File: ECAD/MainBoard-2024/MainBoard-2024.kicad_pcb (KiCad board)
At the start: 2 copper layers, 100 x 100 mm, 65 parts, among them J1 XT60, J10 Conn_01x02, J11 Conn_01x03, J12 Conn_01x04, J13 Conn_01x03, J14 Conn_01x03, J15 Conn_01x02, J16 XT30, J17 XT30, J18 Conn_01x02, J2 Conn_01x04, J20 BAU, J21 BAU, J22 Conn_01x04, J23 Conn_01x02, J26 BAU, J27 BAU, J28 Conn_01x02, J29 Conn_01x02, J3 ConStep1, J30 Conn_01x03, J4 Conn_01x02, J5 ConStep1, J6 ConStep1, J7 XT30, J8 Conn_01x02, J9 Conn_01x02, K2 FINDER-36.11, U1 Teensy3.5_All_Pins, U2 R-78B3.3-2.0, U3 R-78B12-2.0, U4 R-78B5.0-2.0

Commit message: Clean positions
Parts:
- removed J16, J17: XT30, Connector_AMASS:AMASS_XT30U-F_1x02_P5.0mm_Vertical
- moved J27 84.2 mm to (187.3, 70.1)
- moved J20 83.1 mm to (187.3, 58.4)
- moved J26 83.1 mm to (196.9, 58.4)
- moved C4 48.3 mm to (165.1, 68.6)
- moved C6 48.3 mm to (165.1, 58.4)
- moved K2 36.0 mm to (142.3, 133.2), turned to 0 degrees
- moved J1 29.1 mm to (165.6, 137.6), turned to -90 degrees
- moved J21 27.3 mm to (187.5, 141.2)
- moved D1 21.4 mm to (187.2, 102.6)
- moved D3 21.4 mm to (188.5, 107.7)
- moved D5 21.4 mm to (187.2, 100.1)
- moved D6 21.4 mm to (187.2, 95.0)
- moved D8 21.4 mm to (193.5, 107.7)
- moved R1 21.4 mm to (192.4, 102.6)
- moved R17 21.4 mm to (190.8, 107.7)
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
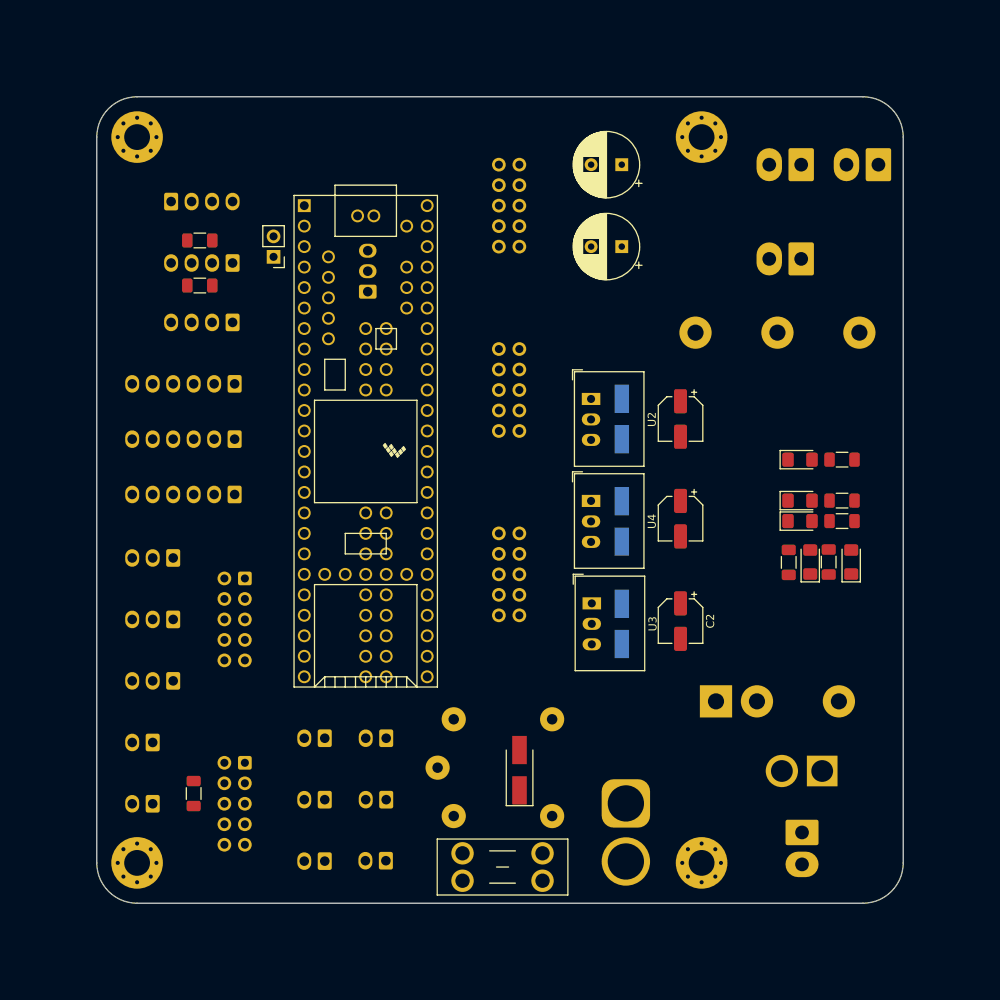
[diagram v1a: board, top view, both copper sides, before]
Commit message: First test trace
PCB Trace with poor optimisation and bad width to check the board before final trace.
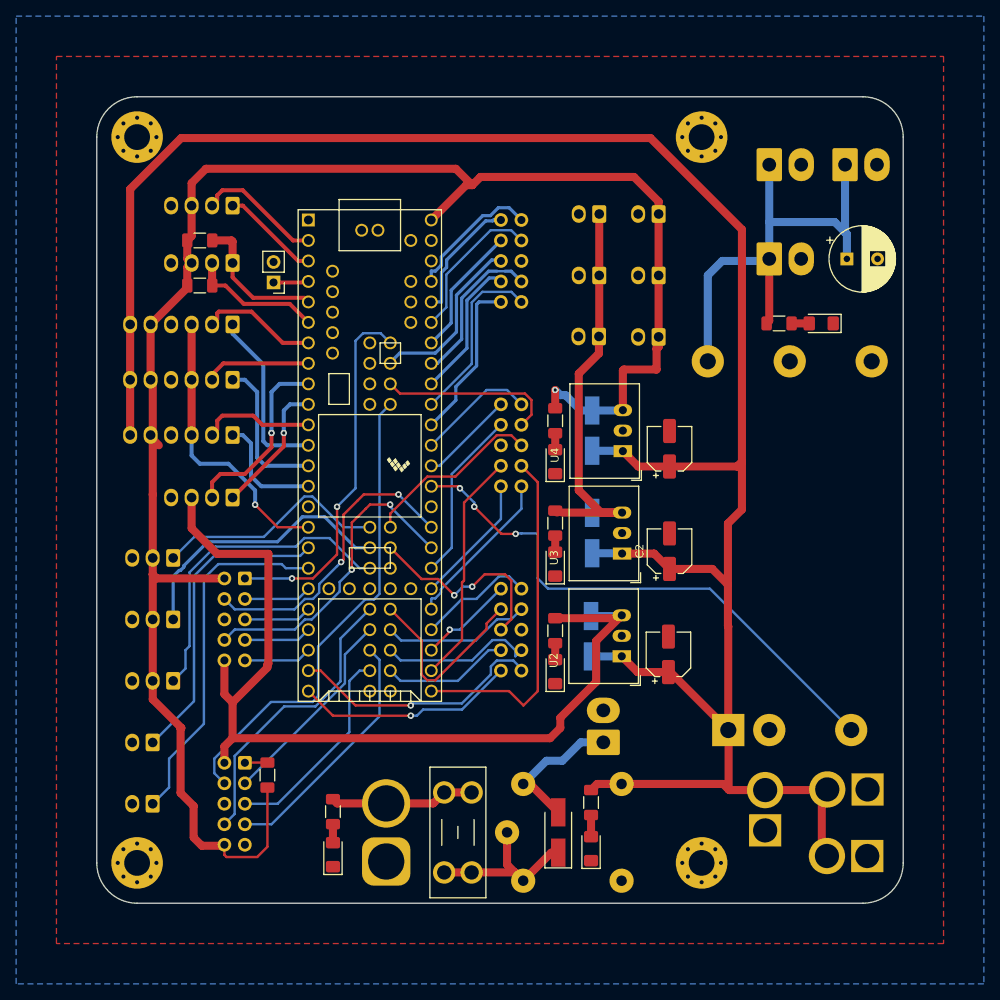
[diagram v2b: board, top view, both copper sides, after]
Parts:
- removed C4: 220uF, Capacitor_THT:CP_Radial_D8.0mm_P3.80mm
- removed J30: Conn_01x03, Connector_Molex:Molex_KK-254_AE-6410-03A_1x03_P2.54mm_Vertical
- added D10: LED_Small, LED_SMD:LED_1206_3216Metric_Pad1.42x1.75mm_HandSolder, F.Cu at (156.8, 108.0)
- added J16: XT30, Connector_AMASS:AMASS_XT30U-F_1x02_P5.0mm_Vertical, B.Cu at (195.5, 144.1)
- added J17: XT30, Connector_AMASS:AMASS_XT30U-F_1x02_P5.0mm_Vertical, B.Cu at (195.6, 135.9)
- added R5: R_Small, Resistor_SMD:R_1206_3216Metric_Pad1.30x1.75mm_HandSolder, F.Cu at (156.8, 102.9)
- moved J10 77.1 mm to (169.7, 79.8)
- moved J4 77.1 mm to (169.7, 64.5)
- moved J9 77.1 mm to (169.7, 72.2)
- moved R3 74.0 mm to (129.3, 138.6), turned to 90 degrees
- moved D5 72.7 mm to (129.3, 144.0), turned to 90 degrees
- moved J23 70.2 mm to (162.3, 72.2)
- moved J29 70.2 mm to (162.3, 64.5)
- moved J28 70.2 mm to (162.3, 79.7)
- moved D1 48.2 mm to (161.3, 143.2), turned to 90 degrees
- moved R1 46.8 mm to (161.3, 137.5), turned to 90 degrees
- moved D8 39.1 mm to (156.8, 121.3)
- moved R17 35.0 mm to (156.8, 116.2), turned to 90 degrees
- moved D3 34.0 mm to (156.8, 95.2)
- moved R2 33.9 mm to (156.8, 90.2), turned to 90 degrees
- moved U2 32.1 mm to (165.1, 119.4), turned to 90 degrees
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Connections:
- IHM-IO1 pad 1: IHM_3 -> NEO_PIXEL
- IHM-IO1 pad 10: DAC0 -> +3V3
- IHM-IO1 pad 3: IHM_4 -> Couleur
- IHM-IO1 pad 4: NEO_PIXEL -> DAC1
- IHM-IO1 pad 7: Couleur -> IHM_3
- IHM-IO1 pad 8: DAC1 -> DAC0
- IHM-IO1 pad 9: +3V3 -> IHM_4
- J11 pad 1: Sensor-01 -> Sensor-02
- J13 pad 1: Sensor-02 -> Sensor-03
- J14 pad 1: Sensor-03 -> Sensor-01
- J15 pad 1: Init -> Tirette
- J18 pad 1: Tirette -> Init
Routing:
- net +24V: track 0.00 -> 279.2 mm
- net +5V: track 0.00 -> 225.9 mm, vias 0 -> 1
- net +3V3: track 0.00 -> 118.4 mm
- net En5VP: track 0.00 -> 68.2 mm, vias 0 -> 3
- net +5VP: track 0.00 -> 61.0 mm
- net TFT_DC: track 0.00 -> 60.2 mm
- net +12V: track 0.00 -> 53.4 mm
- net NEO_PIXEL: track 0.00 -> 45.3 mm, vias 0 -> 2
- net Tirette: track 0.00 -> 44.5 mm
- net C_Act2-4: track 0.00 -> 43.5 mm
- net Sensor-01: track 0.00 -> 40.0 mm
- net DAC0: track 0.00 -> 39.1 mm, vias 0 -> 2
- net Init: track 0.00 -> 38.4 mm
- net DAC1: track 0.00 -> 37.7 mm, vias 0 -> 2
- net TFT_CS: track 0.00 -> 36.4 mm
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- added copper zone on B.Cu, net GND
- added copper zone on F.Cu, net GND

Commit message: Power trace routing
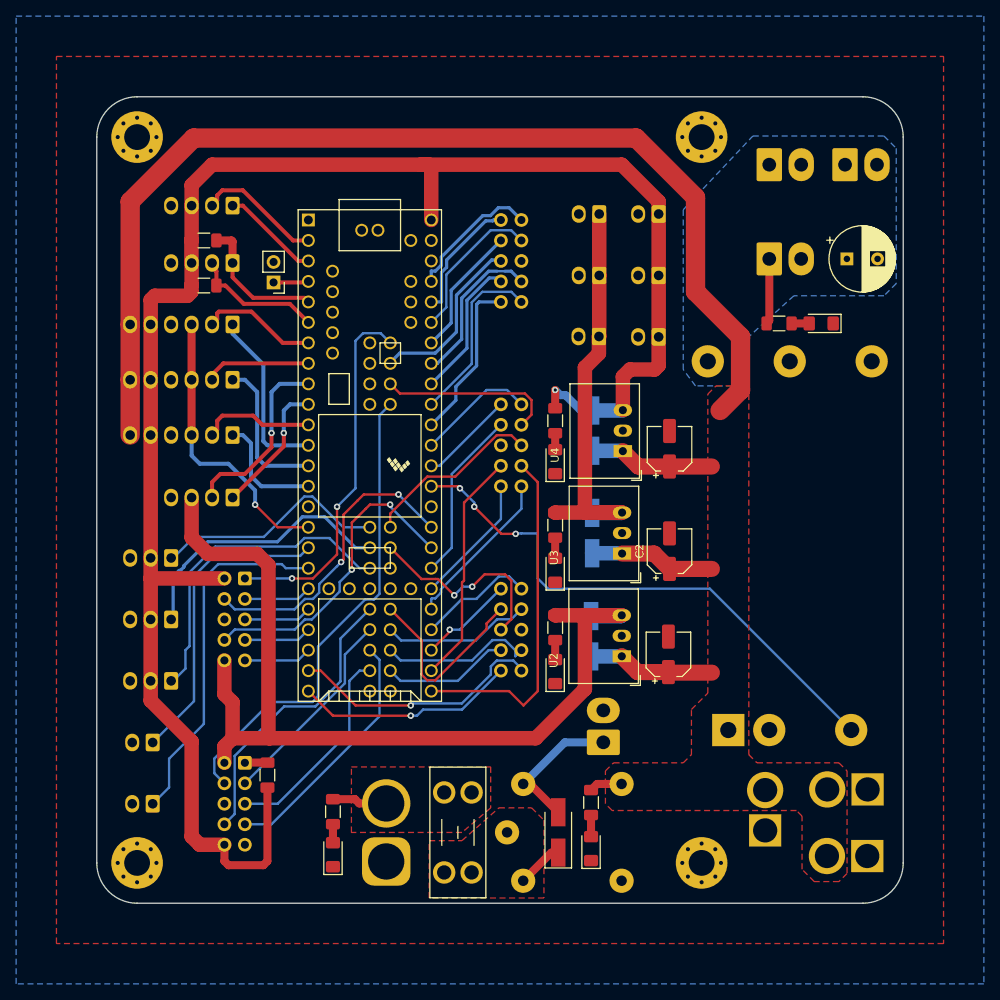
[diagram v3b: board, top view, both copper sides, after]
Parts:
- moved D10 0.76 mm to (156.8, 108.7)
- moved R21 0.51 mm to (113.3, 67.8)
- moved R22 0.51 mm to (113.3, 73.4)
- moved R17 0.38 mm to (156.8, 115.8)
- moved J11 0.25 mm to (109.2, 114.8)
- moved J13 0.25 mm to (109.2, 107.2)
- moved J14 0.25 mm to (109.2, 122.4)
- moved R5 0.25 mm to (156.8, 103.1)
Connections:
- net Net-(D4-K) renamed /24VD
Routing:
- net +24V: track 279.2 -> 186.4 mm
- net +5VP: track 61.0 -> 8.14 mm
- net /24VD: track 22.8 -> 5.79 mm
- net +BATT: track 18.0 -> 6.82 mm
- net +3V3: track 118.4 -> 123.0 mm
- net +5V: track 225.9 -> 228.0 mm
- net +12V: track 53.4 -> 52.3 mm
- net SCL: track 17.7 -> 17.2 mm
- net Net-(D10-A): track 2.04 -> 2.55 mm
- added copper zone on F.Cu, net +24V
- added copper zone on B.Cu, net +5VP
- added copper zone on F.Cu, net +BATT
- added copper zone on F.Cu, net /24VD

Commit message: fix trace width on actionneur connector
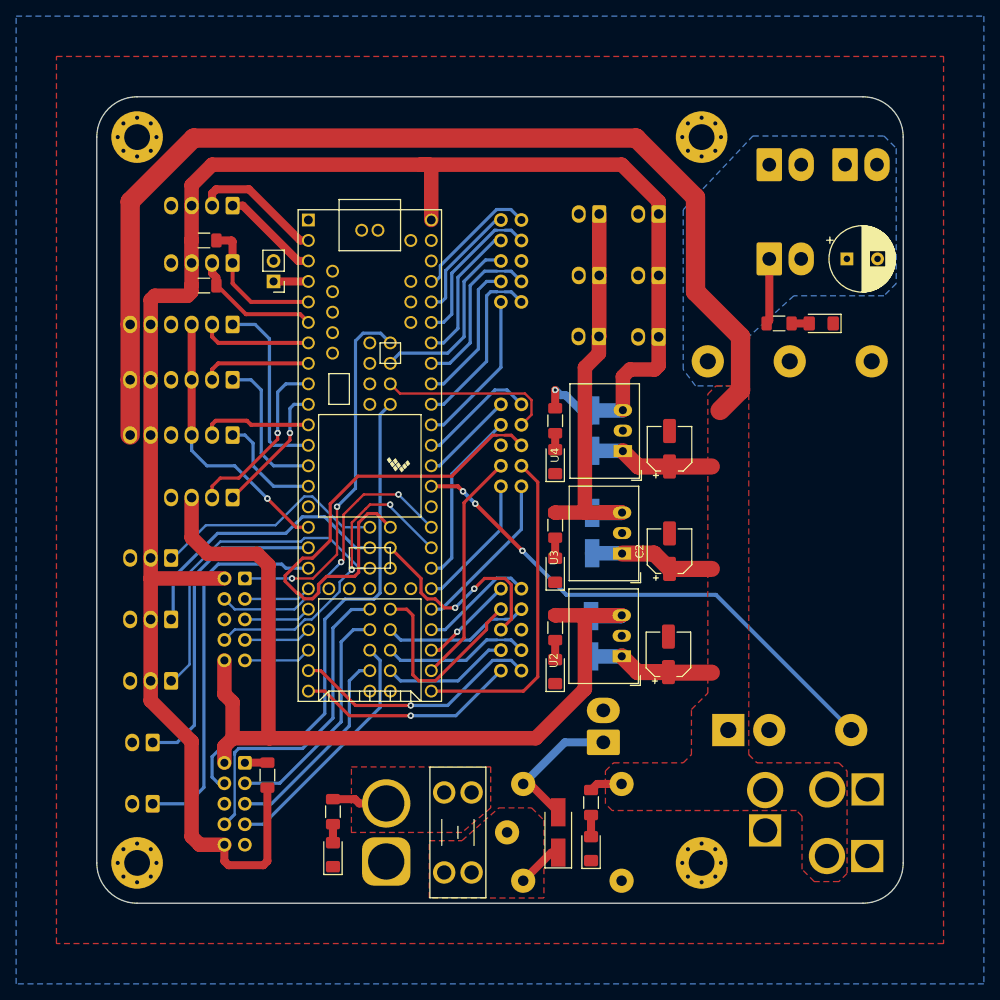
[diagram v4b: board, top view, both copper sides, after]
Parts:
- moved J8 0.13 mm to (121.9, 72.9)
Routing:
- net C_Act2-9: track 22.5 -> 63.6 mm
- net TFT_DC: track 60.2 -> 64.4 mm
- net TFT_MOSI: track 25.5 -> 29.2 mm
- net TFT_CS: track 36.4 -> 40.1 mm
- net En5VP: track 68.2 -> 64.6 mm
- net Tirette: track 44.5 -> 47.0 mm
- net C_Act2-4: track 43.5 -> 40.9 mm
- net C_Act3-5: track 23.9 -> 25.8 mm
- net Init: track 38.4 -> 40.2 mm
- net C_Act3-9: track 25.5 -> 27.1 mm
- net EN: track 35.5 -> 34.0 mm
- net C_Act1-9: track 21.6 -> 23.0 mm
- net C_Act1-5: track 16.3 -> 17.6 mm
- net C_Act1-4: track 19.4 -> 20.6 mm
- net DIR_1: track 21.9 -> 23.0 mm
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
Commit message: fix trace width an position on IHM, TFT and side connectors
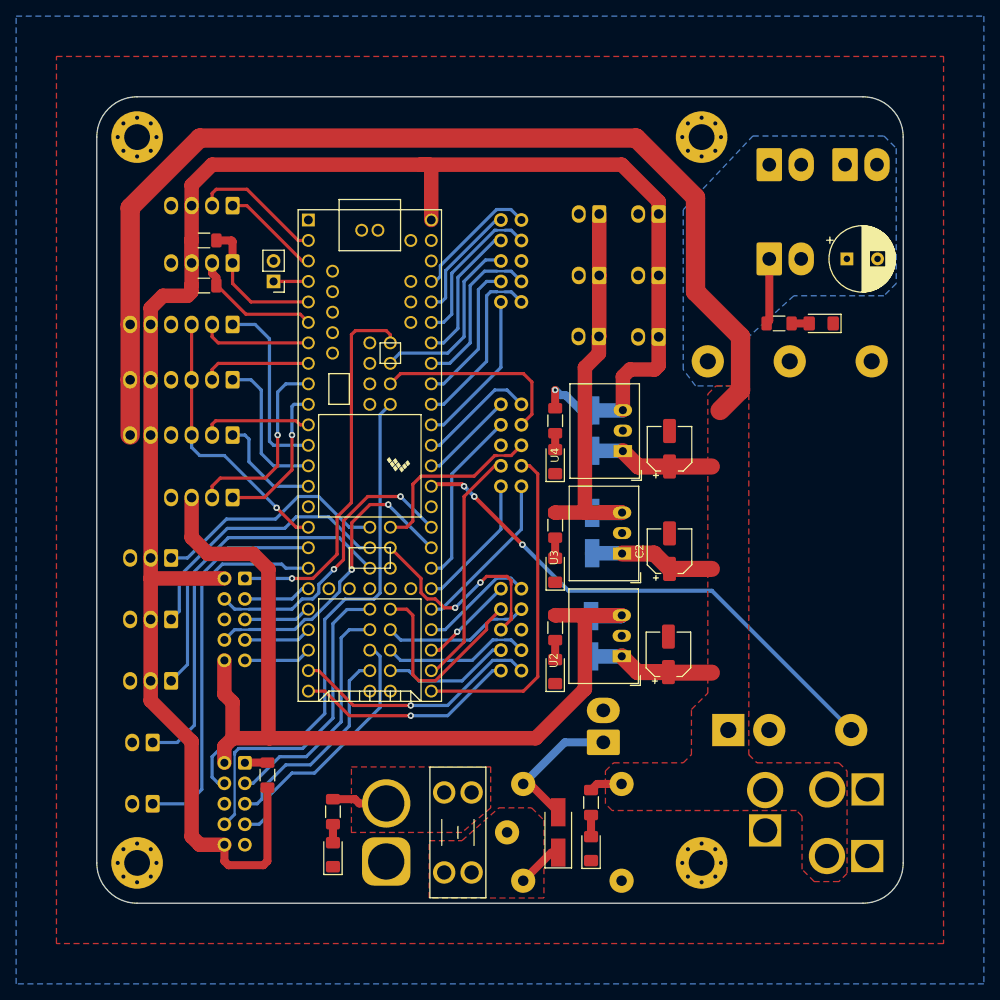
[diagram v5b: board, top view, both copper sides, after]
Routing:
- net C_Act2-9: track 63.6 -> 23.1 mm
- net C_Act2-6: track 21.9 -> 24.4 mm
- net DIN-xbee: track 16.5 -> 18.8 mm
- net DOUT-xbee: track 22.0 -> 24.0 mm
- net TFT_MISO: track 30.4 -> 32.0 mm
- net NEO_PIXEL: track 45.3 -> 46.9 mm, vias 2 -> 1
- net TFT_SCK: track 25.6 -> 26.3 mm
- net C_Act2-3: track 29.0 -> 29.7 mm
- net DAC1: track 37.7 -> 36.9 mm
- net C_Act2-4: track 40.9 -> 41.5 mm
- net +5V: track 228.0 -> 227.4 mm

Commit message: Fix errors and warnings following DRC
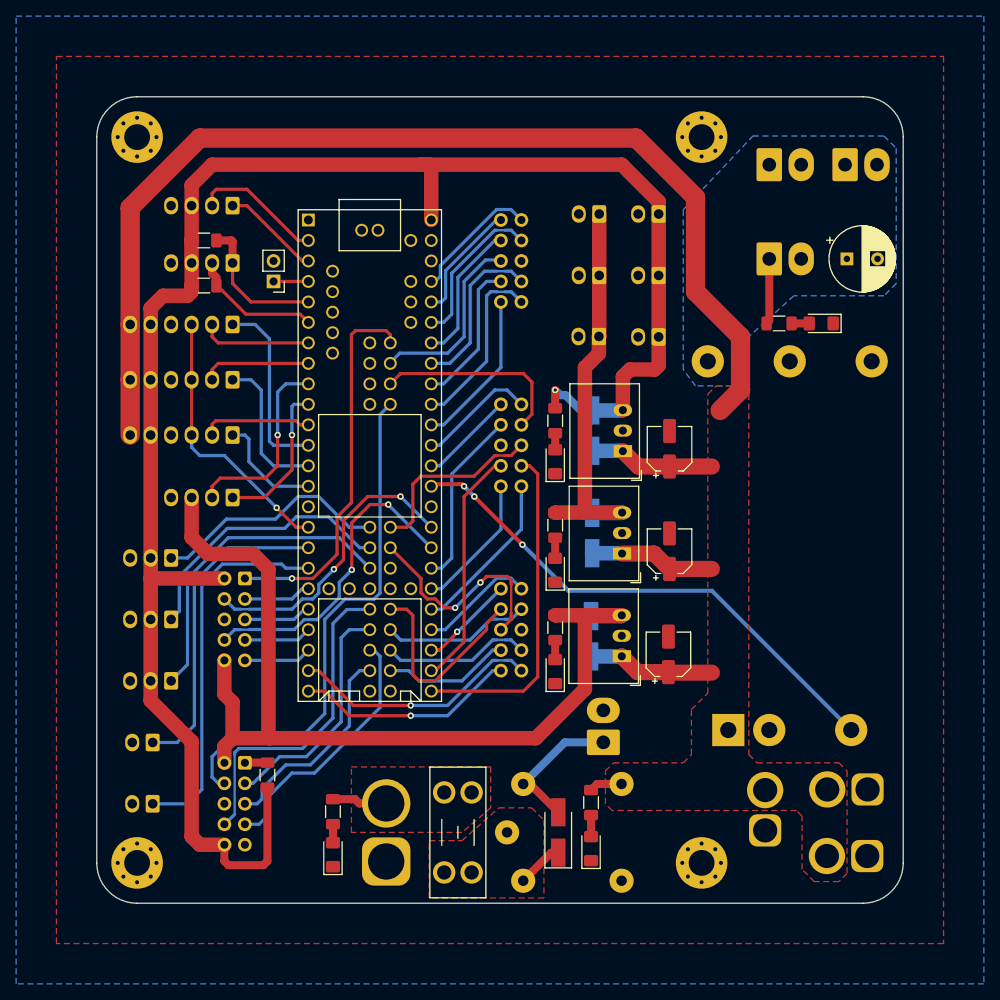
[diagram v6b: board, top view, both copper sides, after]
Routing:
- net +12V: track 52.3 -> 49.8 mm

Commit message: First silkscreen labels
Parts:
- added G***: LOGO, LOGO, B.Cu at (167.1, 60.5)
- added G***: LOGO, LOGO, B.Cu at (159.7, 60.5)
- added G***: LOGO, LOGO, B.Cu at (130.8, 144.8)
- added G***: LOGO, LOGO, B.Cu at (182.9, 144.6)
- added G***: LOGO, LOGO, B.Cu at (170.7, 126.0)
- added G***: LOGO, LOGO, B.Cu at (190.0, 70.1)
- added kibuzzard-64932E55: G***, kibuzzard-64932E55, B.Cu at (162.3, 59.2)
- added kibuzzard-64932EB2: G***, kibuzzard-64932EB2, B.Cu at (169.7, 59.1)
- added kibuzzard-64932F6F: G***, kibuzzard-64932F6F, B.Cu at (178.8, 58.9)
- added kibuzzard-64932F6F: G***, kibuzzard-64932F6F, B.Cu at (178.8, 70.1)
- added kibuzzard-64932FD6: G***, kibuzzard-64932FD6, B.Cu at (128.0, 137.7)
- added kibuzzard-64933096: G***, kibuzzard-64933096, B.Cu at (177.3, 136.1)
- added kibuzzard-64933122: G***, kibuzzard-64933122, B.Cu at (168.5, 101.6)
- added kibuzzard-64933136: G***, kibuzzard-64933136, B.Cu at (168.5, 114.3)
- added kibuzzard-64933140: G***, kibuzzard-64933140, B.Cu at (168.4, 88.9)
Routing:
- added copper zone on B.Cu, net +BATT
- added copper zone on B.Cu, net /24VD
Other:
- board text added: "BAU"

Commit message: Complete Bottom Silkscreen
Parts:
- removed kibuzzard-64932FD6: G***, kibuzzard-64932FD6
- added G***: LOGO, LOGO, B.Cu at (169.2, 53.8)
- added G***: LOGO, LOGO, B.Cu at (109.2, 59.7)
- added kibuzzard-64932EB2: G***, kibuzzard-64932EB2, B.Cu at (111.8, 58.2)
- added kibuzzard-6493EE40: G***, kibuzzard-6493EE40, B.Cu at (121.4, 94.0)
- added kibuzzard-6493EE50: G***, kibuzzard-6493EE50, B.Cu at (121.4, 80.3)
- added kibuzzard-6493EE56: G***, kibuzzard-6493EE56, B.Cu at (121.4, 87.1)
- added kibuzzard-6493EE83: G***, kibuzzard-6493EE83, B.Cu at (106.2, 99.6)
- added kibuzzard-6493EE9E: G***, kibuzzard-6493EE9E, B.Cu at (106.4, 70.6)
- added kibuzzard-6493EEAC: G***, kibuzzard-6493EEAC, B.Cu at (105.9, 63.5)
- added kibuzzard-6493EEE0: G***, kibuzzard-6493EEE0, B.Cu at (114.3, 58.4)
- added kibuzzard-6493EEF0: G***, kibuzzard-6493EEF0, B.Cu at (116.8, 58.4)
- added kibuzzard-6493EF75: G***, kibuzzard-6493EF75, B.Cu at (105.3, 103.4)
- added kibuzzard-6493EFD0: G***, kibuzzard-6493EFD0, B.Cu at (111.5, 107.2)
- added kibuzzard-6493EFE7: G***, kibuzzard-6493EFE7, B.Cu at (111.5, 114.8)
- added kibuzzard-6493EFEC: G***, kibuzzard-6493EFEC, B.Cu at (111.5, 122.4)
- added kibuzzard-6493F09E: G***, kibuzzard-6493F09E, B.Cu at (109.2, 137.7)
- added kibuzzard-6493F0A8: G***, kibuzzard-6493F0A8, B.Cu at (109.2, 130.0)
- added kibuzzard-6493F0C8: G***, kibuzzard-6493F0C8, B.Cu at (135.9, 132.1)
- added kibuzzard-6493F0E7: G***, kibuzzard-6493F0E7, B.Cu at (122.7, 137.9)
- added kibuzzard-6493F100: G***, kibuzzard-6493F100, B.Cu at (122.9, 114.8)
- added kibuzzard-6493F174: G***, kibuzzard-6493F174, B.Cu at (145.8, 67.1)
- added kibuzzard-6493F18B: G***, kibuzzard-6493F18B, B.Cu at (145.8, 89.9)
- added kibuzzard-6493F190: G***, kibuzzard-6493F190, B.Cu at (145.8, 112.8)
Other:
- board text added: "Même connecteurs MAIS tensions différentes"
